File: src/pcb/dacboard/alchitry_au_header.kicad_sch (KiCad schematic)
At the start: 10 parts, among them J14 Conn_01x14, J15 Conn_01x14, J17 Conn_01x14, J18 Conn_01x14, J19 Conn_01x14, J20 Conn_01x14, J21 Conn_01x14, J22 Conn_01x06, J4 Conn_01x14, J6 Conn_01x14

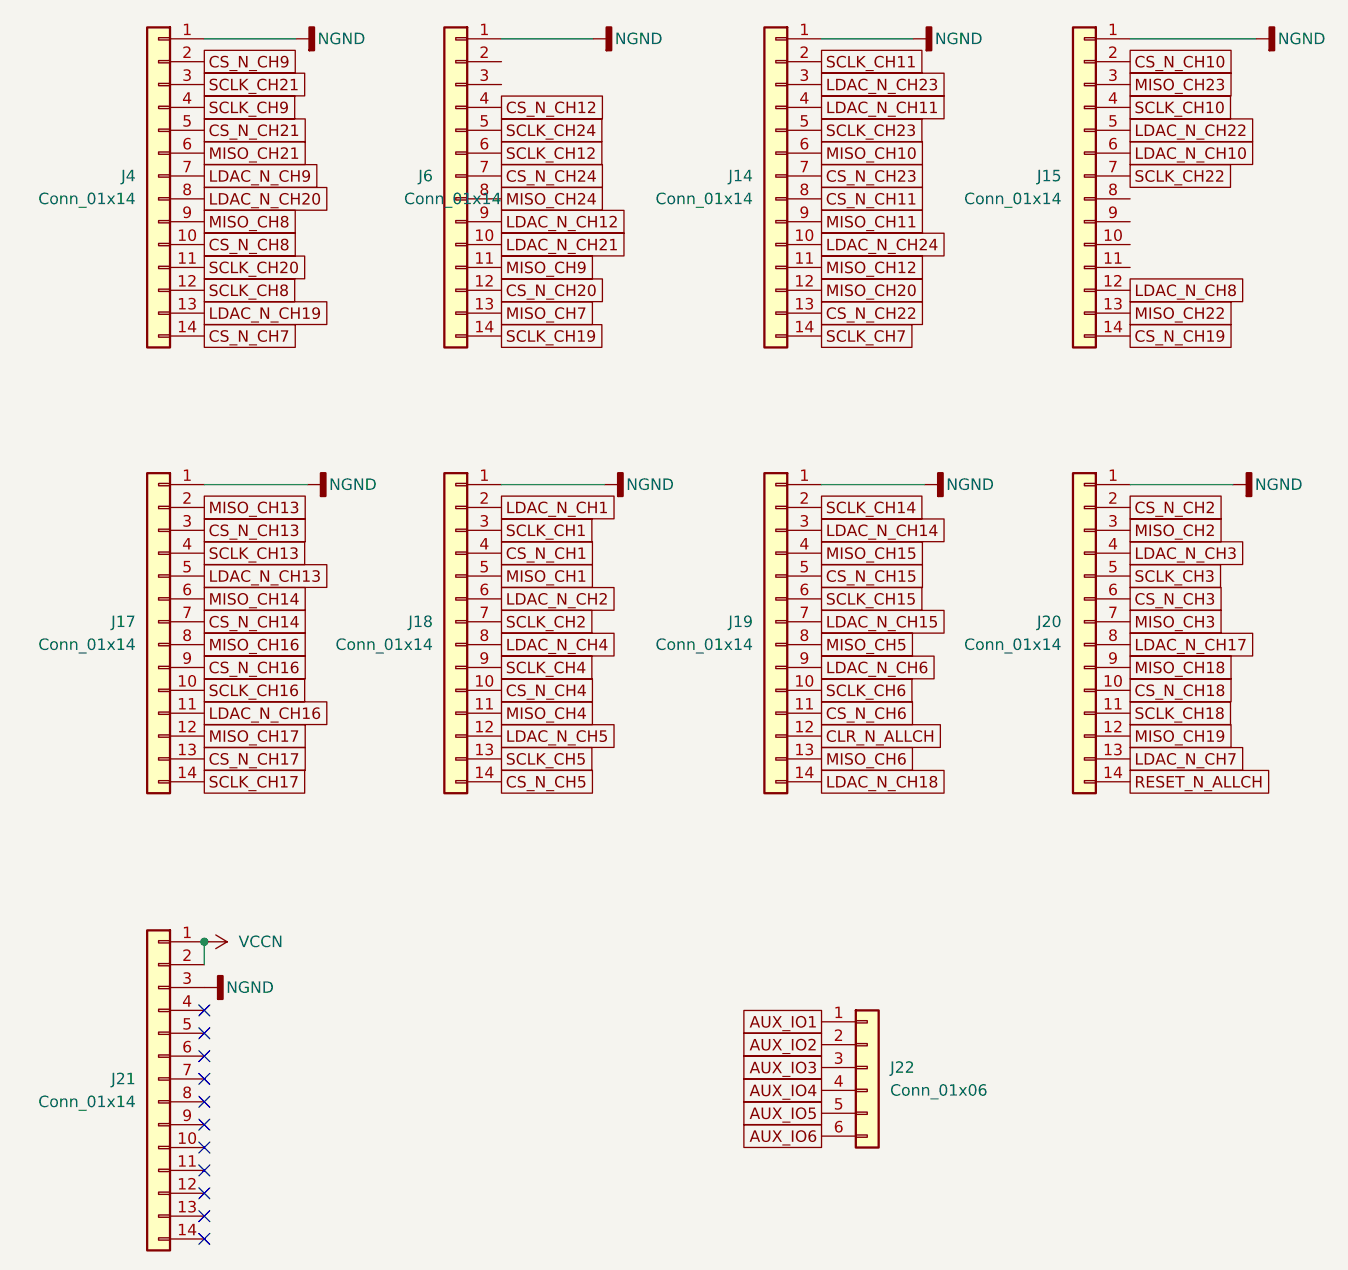
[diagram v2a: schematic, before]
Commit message: got rid of all drc errors
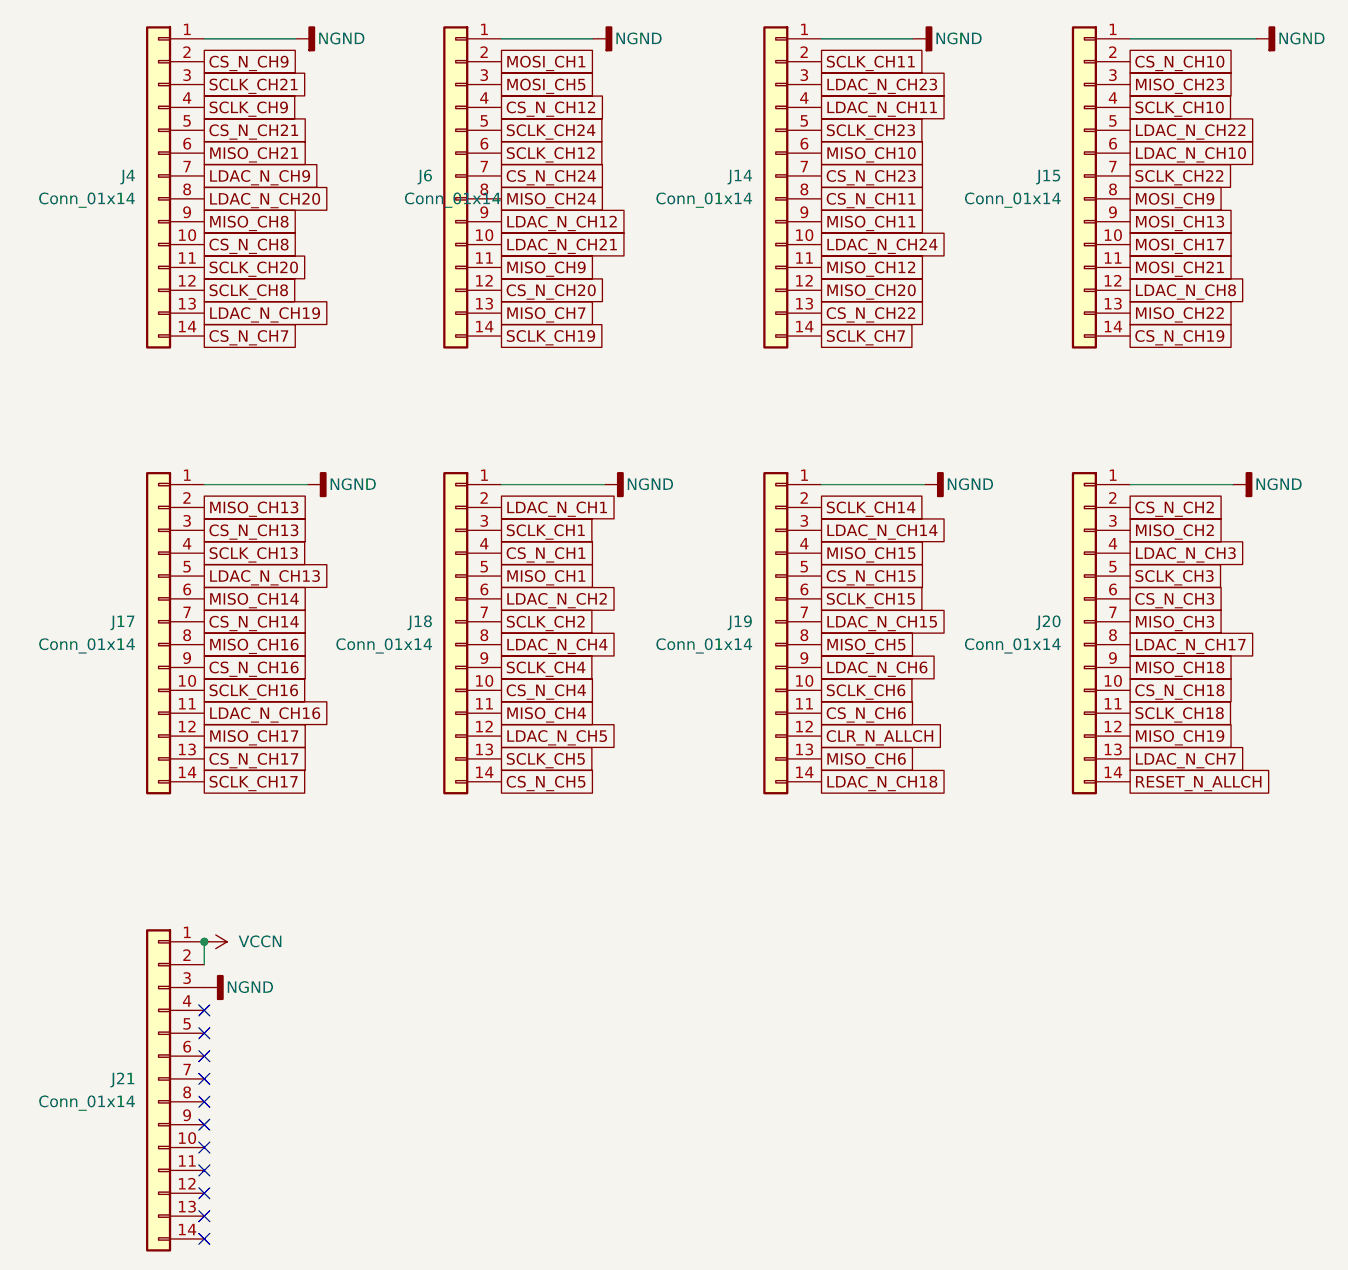
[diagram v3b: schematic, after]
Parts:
- removed J22: Conn_01x06, Connector_PinHeader_2.54mm:PinHeader_1x06_P2.54mm_Vertical, symbol Connector_Generic:Conn_01x06
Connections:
- net MOSI_CH1: now reaches J6.2 (Pin_2)
- net MOSI_CH5: now reaches J6.3 (Pin_3)
- net MOSI_CH17: now reaches J15.10 (Pin_10)
- net MOSI_CH21: now reaches J15.11 (Pin_11)
- net MOSI_CH9: now reaches J15.8 (Pin_8)
- net MOSI_CH13: now reaches J15.9 (Pin_9)
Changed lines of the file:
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@@
+		)
+	)
+	(global_label "MOSI_CH1"
+		(shape passive)
+		(at 96.52 24.13 0)
+		(fields_autoplaced yes)
+		(effects
+			(font
+				(size 1.27 1.27)
+			)
+			(justify left)
+		)
+		(property "Intersheetrefs" "${INTERSHEET_REFS}"
+			(at 107.7677 24.13 0)
+			(effects
+				(font
+					(size 1.27 1.27)
+				)
+				(justify left)
+				(hide yes)
+			)
 		)
 	)
@@
 		)
 	)
-	(global_label "AUX_IO1"
-		(shape passive)
-		(at 132.08 130.81 180)
-		(fields_autoplaced yes)
-		(effects
-			(font
-				(size 1.27 1.27)
-			)
-			(justify right)
-		)
-		(property "Intersheetrefs" "${INTERSHEET_REFS}"
-			(at 122.4651 130.81 0)
-			(effects
-				(font
-					(size 1.27 1.27)
-				)
-				(justify right)
-				(hide yes)
-			)
-		)
-	)
-	(global_label "AUX_IO4"
-		(shape passive)
-		(at 132.08 138.43 180)
-		(fields_autoplaced yes)
-		(effects
-			(font
-				(size 1.27 1.27)
-			)
-			(justify right)
-		)
-		(property "Intersheetrefs" "${INTERSHEET_REFS}"
-			(at 122.4651 138.43 0)
-			(effects
-				(font
-					(size 1.27 1.27)
-				)
-				(justify right)
-				(hide yes)
-			)
-		)
-	)
 	(global_label "SCLK_CH9"
 		(shape passive)
@@
 		)
 	)
-	(global_label "AUX_IO5"
-		(shape passive)
-		(at 132.08 140.97 180)
-		(fields_autoplaced yes)
-		(effects
-			(font
-				(size 1.27 1.27)
-			)
-			(justify right)
-		)
-		(property "Intersheetrefs" "${INTERSHEET_REFS}"
-			(at 122.4651 140.97 0)
-			(effects
-				(font
-					(size 1.27 1.27)
-				)
-				(justify right)
-				(hide yes)
-			)
-		)
-	)
 	(global_label "LDAC_N_CH14"
 		(shape passive)
@@
 		)
 	)
+	(global_label "MOSI_CH17"
+		(shape passive)
+		(at 166.37 44.45 0)
+		(fields_autoplaced yes)
+		(effects
+			(font
+				(size 1.27 1.27)
+			)
+			(justify left)
+		)
+		(property "Intersheetrefs" "${INTERSHEET_REFS}"
+			(at 178.8272 44.45 0)
+			(effects
+				(font
+					(size 1.27 1.27)
+				)
+				(justify left)
+				(hide yes)
+			)
+		)
+	)
 	(global_label "MISO_CH11"
 		(shape passive)
@@
 		)
 	)
-	(global_label "AUX_IO6"
-		(shape passive)
-		(at 132.08 143.51 180)
-		(fields_autoplaced yes)
-		(effects
-			(font
-				(size 1.27 1.27)
-			)
-			(justify right)
-		)
-		(property "Intersheetrefs" "${INTERSHEET_REFS}"
-			(at 122.4651 143.51 0)
-			(effects
-				(font
-					(size 1.27 1.27)
-				)
-				(justify right)
-				(hide yes)
-			)
-		)
-	)
 	(global_label "MISO_CH16"
 		(shape passive)
@@
 		)
 	)
+	(global_label "MOSI_CH5"
+		(shape passive)
+		(at 96.52 26.67 0)
+		(fields_autoplaced yes)
+		(effects
+			(font
+				(size 1.27 1.27)
+			)
+			(justify left)
+		)
+		(property "Intersheetrefs" "${INTERSHEET_REFS}"
+			(at 107.7677 26.67 0)
+			(effects
+				(font
+					(size 1.27 1.27)
+				)
+				(justify left)
+				(hide yes)
+			)
+		)
+	)
 	(global_label "MISO_CH19"
 		(shape passive)
@@
 		)
 	)
+	(global_label "MOSI_CH21"
+		(shape passive)
+		(at 166.37 46.99 0)
+		(fields_autoplaced yes)
+		(effects
+			(font
+				(size 1.27 1.27)
+			)
+			(justify left)
+		)
+		(property "Intersheetrefs" "${INTERSHEET_REFS}"
+			(at 178.8272 46.99 0)
+			(effects
+				(font
+					(size 1.27 1.27)
+				)
+				(justify left)
+				(hide yes)
+			)
+		)
+	)
 	(global_label "CS_N_CH1"
 		(shape passive)
@@
 		)
 	)
+	(global_label "MOSI_CH13"
+		(shape passive)
+		(at 166.37 41.91 0)
+		(fields_autoplaced yes)
+		(effects
+			(font
+				(size 1.27 1.27)
+			)
+			(justify left)
+		)
+		(property "Intersheetrefs" "${INTERSHEET_REFS}"
+			(at 178.8272 41.91 0)
+			(effects
+				(font
+					(size 1.27 1.27)
+				)
+				(justify left)
+				(hide yes)
+			)
+		)
+	)
 	(global_label "CS_N_CH22"
 		(shape passive)
@@
 		)
 	)
-	(global_label "AUX_IO2"
-		(shape passive)
-		(at 132.08 133.35 180)
-		(fields_autoplaced yes)
-		(effects
-			(font
-				(size 1.27 1.27)
-			)
-			(justify right)
-		)
-		(property "Intersheetrefs" "${INTERSHEET_REFS}"
-			(at 122.4651 133.35 0)
-			(effects
-				(font
-					(size 1.27 1.27)
-				)
-				(justify right)
-				(hide yes)
-			)
-		)
-	)
 	(global_label "LDAC_N_CH22"
 		(shape passive)
@@
 		)
 	)
+	(global_label "MOSI_CH9"
+		(shape passive)
+		(at 166.37 39.37 0)
+		(fields_autoplaced yes)
+		(effects
+			(font
+				(size 1.27 1.27)
+			)
+			(justify left)
+		)
+		(property "Intersheetrefs" "${INTERSHEET_REFS}"
+			(at 177.6177 39.37 0)
+			(effects
+				(font
+					(size 1.27 1.27)
+				)
+				(justify left)
+				(hide yes)
+			)
+		)
+	)
 	(global_label "LDAC_N_CH3"
 		(shape passive)
@@
 				)
 				(justify left)
-				(hide yes)
-			)
-		)
-	)
-	(global_label "AUX_IO3"
-		(shape passive)
-		(at 132.08 135.89 180)
-		(fields_autoplaced yes)
-		(effects
-			(font
-				(size 1.27 1.27)
-			)
-			(justify right)
-		)
-		(property "Intersheetrefs" "${INTERSHEET_REFS}"
-			(at 122.4651 135.89 0)
-			(effects
-				(font
-					(size 1.27 1.27)
-				)
-				(justify right)
 				(hide yes)
 			)
@@
 					(unit 1)
 				)
-			)
-		)
-	)
-	(symbol
-		(lib_id "Connector_Generic:Conn_01x06")
-		(at 137.16 135.89 0)
-		(unit 1)
-		(exclude_from_sim no)
-		(in_bom yes)
-		(on_board yes)
-		(dnp no)
-		(fields_autoplaced yes)
-		(property "Reference" "J22"
-			(at 139.7 135.8899 0)
-			(effects
-				(font
-					(size 1.27 1.27)
-				)
-				(justify left)
-			)
-		)
-		(property "Value" "Conn_01x06"
-			(at 139.7 138.4299 0)
-			(effects
-				(font
-					(size 1.27 1.27)
-				)
-				(justify left)
-			)
-		)
-		(property "Footprint" "Connector_PinHeader_2.54mm:PinHeader_1x06_P2.54mm_Vertical"
-			(at 137.16 135.89 0)
-			(effects
-				(font
-					(size 1.27 1.27)
-				)
-				(hide yes)
-			)
-		)
-		(property "Datasheet" "~"
-			(at 137.16 135.89 0)
-			(effects
-				(font
-					(size 1.27 1.27)
-				)
-				(hide yes)
-			)
-		)
-		(property "Description" "Generic connector, single row, 01x06, script generated (kicad-library-utils/schlib/autogen/connector/)"
-			(at 137.16 135.89 0)
-			(effects
-				(font
-					(size 1.27 1.27)
-				)
-				(hide yes)
-			)
-		)
-		(pin "3"
-		)
-		(pin "4"
-		)
-		(pin "5"
-		)
-		(pin "6"
-		)
-		(pin "2"
-		)
-		(pin "1"
-		)
-		(instances
-			(project ""
-				(path "/35cb74e4-0f64-454b-9b50-bfac13ed28a5/7ae8c1dd-5c28-4985-bc49-d575e389aef0/3a359f7d-847e-4fe9-b2d0-8ca1a5344520"
-					(reference "J22")
-					(unit 1)
-				)

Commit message: dacboard au aux ports
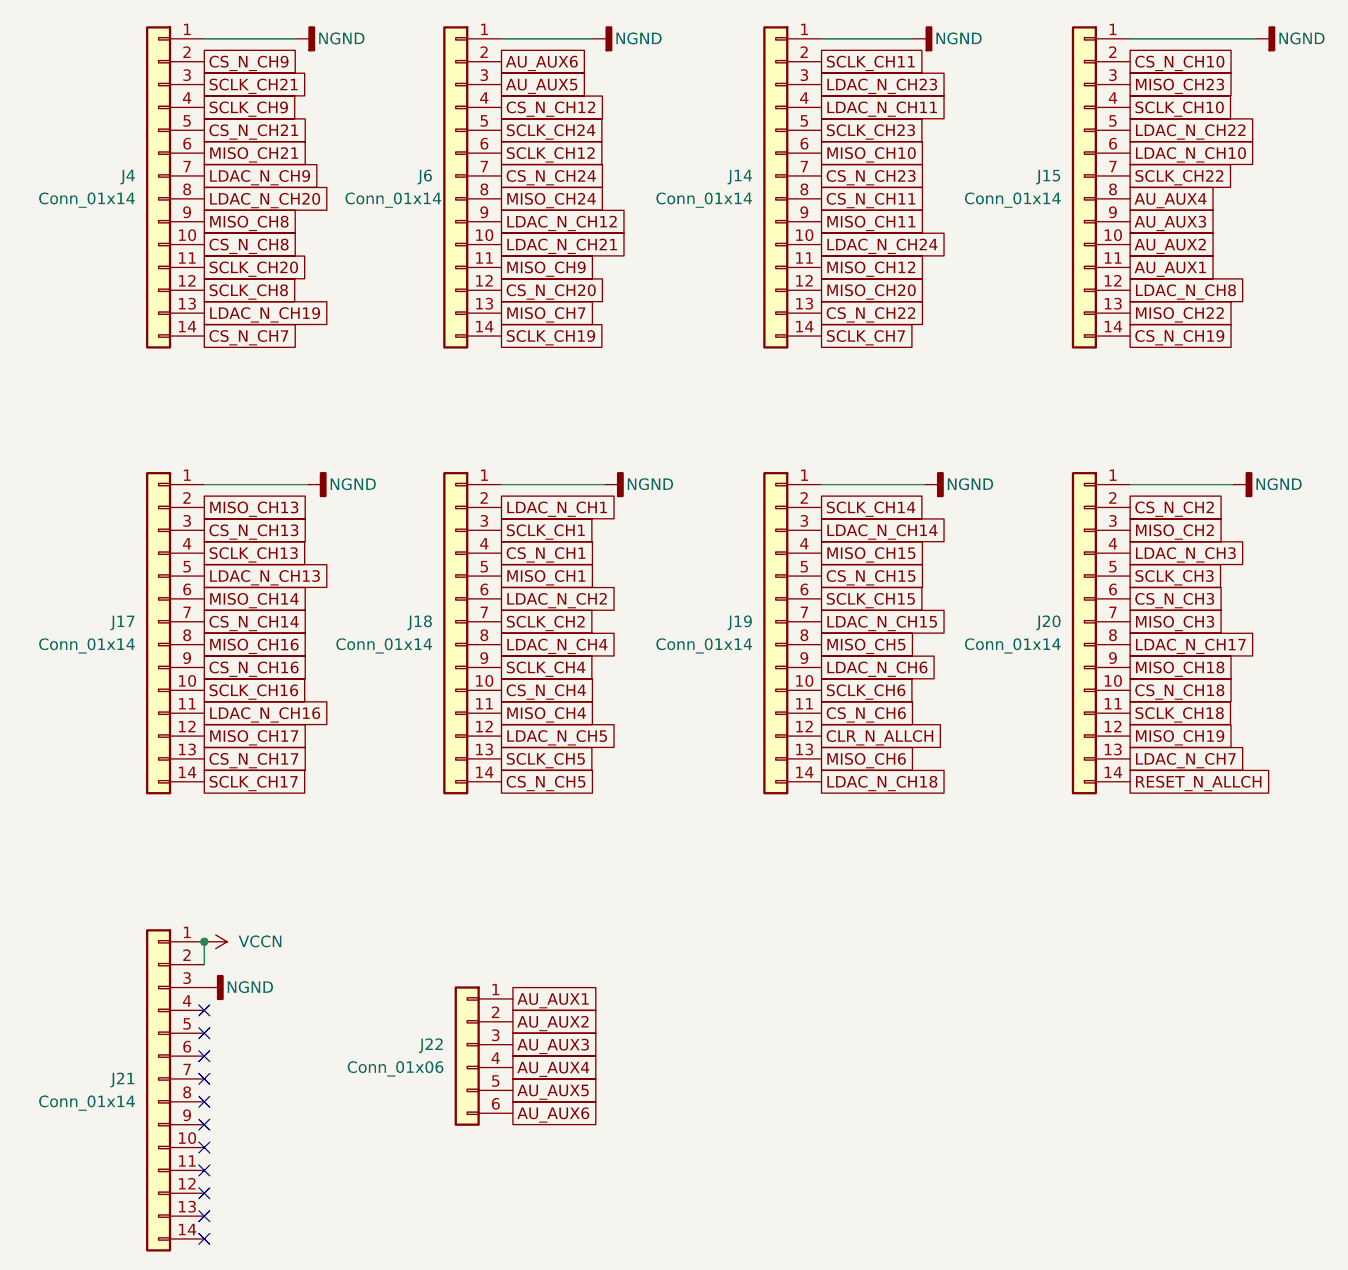
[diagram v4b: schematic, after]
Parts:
- added J22: Conn_01x06, Connector_PinHeader_2.54mm:PinHeader_1x06_P2.54mm_Vertical, symbol Connector_Generic:Conn_01x06
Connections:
- net MOSI_CH1 renamed AU_AUX6
- net AU_AUX6: now also J22.6 (Pin_6)
- net MOSI_CH13 renamed AU_AUX3
- net AU_AUX3: now also J22.3 (Pin_3)
- net MOSI_CH17 renamed AU_AUX2
- net AU_AUX2: now also J22.2 (Pin_2)
- net MOSI_CH21 renamed AU_AUX1
- net AU_AUX1: now also J22.1 (Pin_1)
- net MOSI_CH5 renamed AU_AUX5
- net AU_AUX5: now also J22.5 (Pin_5)
- net MOSI_CH9 renamed AU_AUX4
- net AU_AUX4: now also J22.4 (Pin_4)
